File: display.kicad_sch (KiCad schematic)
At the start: 72 parts, among them IC11 SN74LV1T125DBVR, IC6 PCA9517ADP, J1 46756-1001, J2 2129320-3, T1 BSS138APW

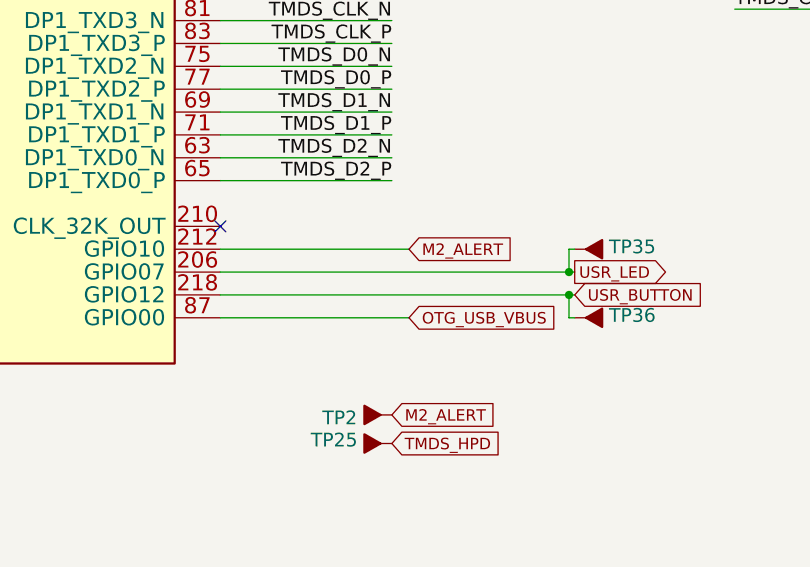
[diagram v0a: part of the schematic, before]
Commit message: Connect OTG VBUS_DET and ID_DET signals to SOM
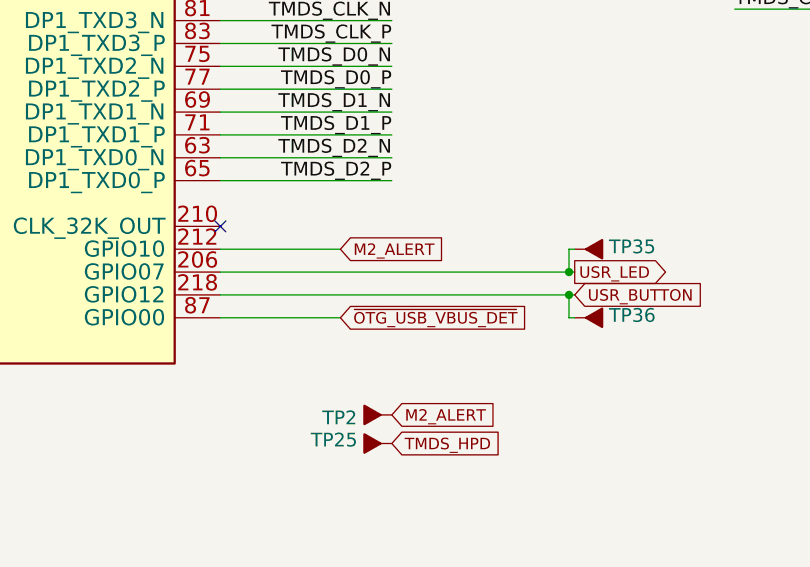
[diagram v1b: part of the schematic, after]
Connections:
- net OTG_USB_VBUS renamed ~{OTG_USB_VBUS_DET}
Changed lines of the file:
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@@
     (stroke (width 0) (type default) (color 0 0 0 0))
   )
-  (wire (pts (xy 63.5 121.92) (xy 84.455 121.92))
+  (wire (pts (xy 63.5 121.92) (xy 76.835 121.92))
     (stroke (width 0) (type default) (color 0 0 0 0))
   )
@@
     (stroke (width 0) (type default) (color 0 0 0 0))
   )
-  (wire (pts (xy 63.5 114.3) (xy 84.455 114.3))
+  (wire (pts (xy 63.5 114.3) (xy 76.835 114.3))
     (stroke (width 0) (type default) (color 0 0 0 0))
   )
@@
     )
   )
-  (global_label "M2_ALERT" (shape input) (at 84.455 114.3 0) (fields_autoplaced)
+  (global_label "M2_ALERT" (shape input) (at 76.835 114.3 0) (fields_autoplaced)
     (effects (font (size 1.27 1.27)) (justify left))
-    (property "Intersheet References" "${INTERSHEET_REFS}" (id 0) (at 0 0 0)
+    (property "Intersheet References" "${INTERSHEET_REFS}" (id 0) (at -7.62 0 0)
       (effects (font (size 1.27 1.27)) hide)
     )
@@
     )
   )
-  (global_label "1V8_SYS" (shape input) (at 236.855 217.805 90) (fields_autoplaced)
+  (global_label "~{OTG_USB_VBUS_DET}" (shape input) (at 76.835 121.92 0) (fields_autoplaced)
     (effects (font (size 1.27 1.27)) (justify left))
-    (property "Intersheet References" "${INTERSHEET_REFS}" (id 0) (at 0 0 0)
-      (effects (font (size 1.27 1.27)) hide)
+    (property "Intersheet References" "${INTERSHEET_REFS}" (id 0) (at 97.7254 121.8406 0)
+      (effects (font (size 1.27 1.27)) (justify left) hide)
     )
   )
-  (global_label "OTG_USB_VBUS" (shape input) (at 84.455 121.92 0) (fields_autoplaced)
+  (global_label "1V8_SYS" (shape input) (at 236.855 217.805 90) (fields_autoplaced)
     (effects (font (size 1.27 1.27)) (justify left))
     (property "Intersheet References" "${INTERSHEET_REFS}" (id 0) (at 0 0 0)

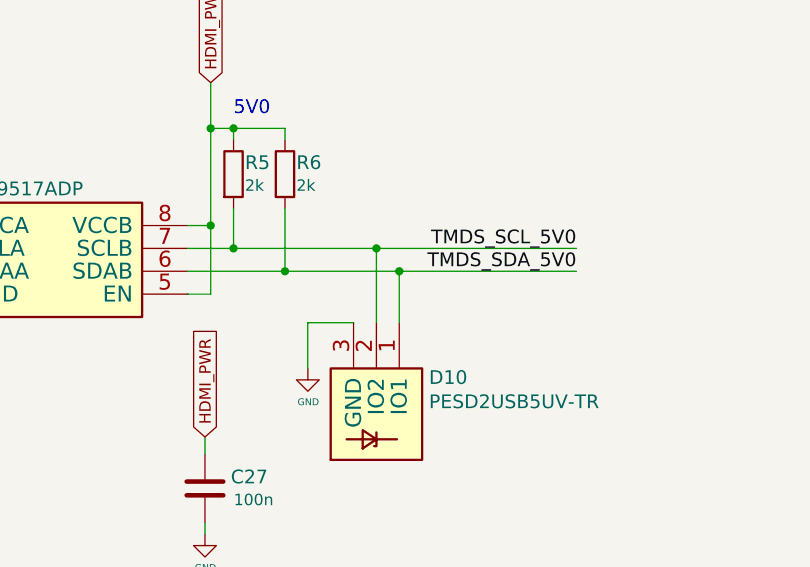
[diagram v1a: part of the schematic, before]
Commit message: Update VBUS_DET label
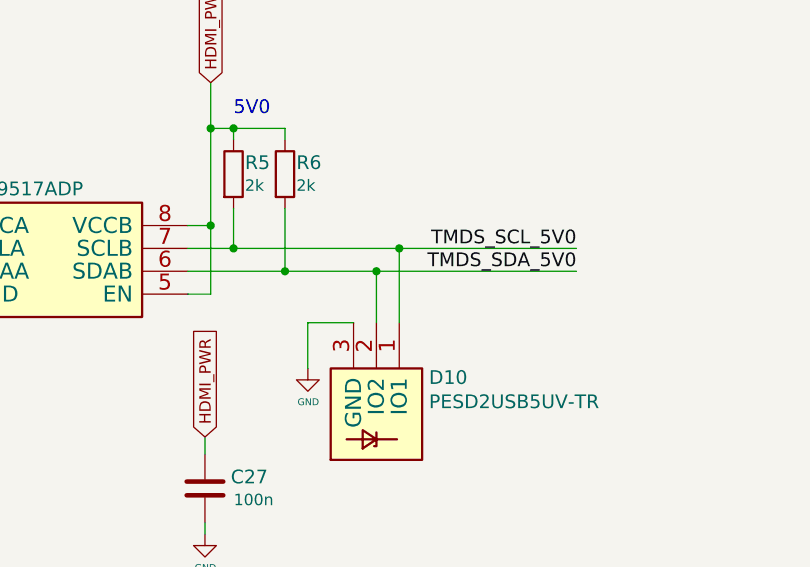
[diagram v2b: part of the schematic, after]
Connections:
- net TMDS_SCL_5V0: now also D10.1 (IO1); no longer D10.2 (IO2)
- net TMDS_SDA_5V0: now also D10.2 (IO2); no longer D10.1 (IO1)
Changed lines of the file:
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@@
   (junction (at 93.345 260.35) (diameter 0) (color 0 0 0 0)
   )
-  (junction (at 367.665 174.625) (diameter 0) (color 0 0 0 0)
-  )
   (junction (at 346.71 169.545) (diameter 0) (color 0 0 0 0)
   )
@@
   (junction (at 300.99 90.805) (diameter 0) (color 0 0 0 0)
   )
+  (junction (at 365.125 174.625) (diameter 0) (color 0 0 0 0)
+  )
+  (junction (at 367.665 172.085) (diameter 0) (color 0 0 0 0)
+  )
   (junction (at 116.205 190.5) (diameter 0) (color 0 0 0 0)
   )
@@
   )
   (junction (at 292.735 90.805) (diameter 0) (color 0 0 0 0)
-  )
-  (junction (at 365.125 172.085) (diameter 0) (color 0 0 0 0)
   )
   (junction (at 354.965 174.625) (diameter 0) (color 0 0 0 0)
@@
     (stroke (width 0) (type default) (color 0 0 0 0))
   )
-  (wire (pts (xy 354.965 174.625) (xy 367.665 174.625))
-    (stroke (width 0) (type default) (color 0 0 0 0))
-  )
   (wire (pts (xy 236.855 218.44) (xy 250.825 218.44))
     (stroke (width 0) (type default) (color 0 0 0 0))
@@
     (stroke (width 0) (type default) (color 0 0 0 0))
   )
+  (wire (pts (xy 365.125 174.625) (xy 365.125 180.34))
+    (stroke (width 0) (type default) (color 0 0 0 0))
+  )
   (wire (pts (xy 313.69 177.165) (xy 313.69 180.34))
     (stroke (width 0) (type default) (color 0 0 0 0))
@@
     (stroke (width 0) (type default) (color 0 0 0 0))
   )
+  (wire (pts (xy 367.665 172.085) (xy 387.35 172.085))
+    (stroke (width 0) (type default) (color 0 0 0 0))
+  )
   (wire (pts (xy 354.33 85.725) (xy 308.61 85.725))
     (stroke (width 0) (type default) (color 0 0 0 0))
   )
-  (wire (pts (xy 365.125 180.34) (xy 365.125 172.085))
-    (stroke (width 0) (type default) (color 0 0 0 0))
-  )
   (wire (pts (xy 90.805 215.9) (xy 149.225 215.9))
     (stroke (width 0) (type default) (color 0 0 0 0))
@@
     (stroke (width 0) (type default) (color 0 0 0 0))
   )
-  (wire (pts (xy 367.665 180.34) (xy 367.665 174.625))
-    (stroke (width 0) (type default) (color 0 0 0 0))
-  )
   (wire (pts (xy 354.33 60.325) (xy 308.61 60.325))
     (stroke (width 0) (type default) (color 0 0 0 0))
@@
     (stroke (width 0) (type default) (color 0 0 0 0))
   )
-  (wire (pts (xy 367.665 174.625) (xy 387.35 174.625))
+  (wire (pts (xy 354.965 174.625) (xy 365.125 174.625))
     (stroke (width 0) (type default) (color 0 0 0 0))
   )
@@
     (stroke (width 0) (type default) (color 0 0 0 0))
   )
-  (wire (pts (xy 349.25 172.085) (xy 365.125 172.085))
-    (stroke (width 0) (type default) (color 0 0 0 0))
-  )
   (wire (pts (xy 118.745 260.35) (xy 116.205 260.35))
     (stroke (width 0) (type default) (color 0 0 0 0))
@@
     (stroke (width 0) (type default) (color 0 0 0 0))
   )
+  (wire (pts (xy 365.125 174.625) (xy 387.35 174.625))
+    (stroke (width 0) (type default) (color 0 0 0 0))
+  )
   (wire (pts (xy 356.235 224.79) (xy 374.65 224.79))
     (stroke (width 0) (type default) (color 0 0 0 0))
@@
     (stroke (width 0) (type default) (color 0 0 0 0))
   )
-  (wire (pts (xy 365.125 172.085) (xy 387.35 172.085))
+  (wire (pts (xy 349.25 172.085) (xy 367.665 172.085))
     (stroke (width 0) (type default) (color 0 0 0 0))
   )
@@
     (stroke (width 0) (type default) (color 0 0 0 0))
   )
+  (wire (pts (xy 367.665 172.085) (xy 367.665 180.34))
+    (stroke (width 0) (type default) (color 0 0 0 0))
+  )

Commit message: Standardize components
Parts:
- removed J2: 2129320-3, jetson-nano-baseboard-footprints:2129320-3, symbol jetson-nano-baseboard:miniDP
- removed R31, R32: R_1M0_0402, jetson-nano-baseboard-footprints:0402-res, symbol jetson-nano-baseboard:R_1M0_0402
- added J2: DisplayPort_Mini_TE_2129320-3, antmicro-footprints:DisplayPort_Mini_TE_2129320-3, symbol antmicroUSBDVIHDMIConnectors:DisplayPort_Mini_TE_2129320-3
- added R31, R32: R_1M_0402, antmicro-footprints:R_0402_1005Metric, symbol antmicroResistors0402:R_1M_0402
- C1, C2, C3, C4: footprint jetson-nano-baseboard-footprints:0402-cap -> antmicro-footprints:C_0402_1005Metric; symbol jetson-nano-baseboard:C_4u7_0402 -> antmicroCapacitors0402:C_4u7_0402; Author (none) -> Antmicro; License (none) -> Apache-2.0; Manufacturer MURATA -> Murata
- C12, C26, C27, C39, C40, C42, C43, C44, C45, C5, C6, C7, C73, C74, C75, C76, C77, C78, C79, C8, C80: footprint jetson-nano-baseboard-footprints:0402-cap -> antmicro-footprints:C_0402_1005Metric; symbol jetson-nano-baseboard:C_100n_0402 -> antmicroCapacitors0402:C_100n_0402; Author (none) -> Antmicro; Dielectric (none) -> X5R; License (none) -> Apache-2.0; MPN 0402X104K6R3CT -> GRM155R61H104KE14D; Manufacturer Walsin -> Murata; Voltage (none) -> 50V
- D10, D11, D12: footprint jetson-nano-baseboard-footprints:SOT-23s -> antmicro-footprints:SOT-23-3; symbol jetson-nano-baseboard:PESD2USB5UV-TR -> antmicroTVSDiodes:PESD2USB5UV-TR; Author (none) -> Antmicro; License (none) -> Apache-2.0; Manufacturer Nexperia -> Nexperia
- D2, D4: footprint jetson-nano-baseboard-footprints:SOD-323 -> antmicro-footprints:D_SOD-323F; symbol jetson-nano-baseboard:diode -> antmicroDiodesRectifiersSingle:1N4148WS; Author (none) -> Antmicro; License (none) -> Apache-2.0
- IC11: footprint jetson-nano-baseboard-footprints:SOT-23-5 -> antmicro-footprints:SOT-23-5; symbol jetson-nano-baseboard:SN74LV1T125DBVR -> antmicroLogicBuffersDriversReceiversTransceivers:SN74LV1T125DBVR; Author (none) -> Antmicro; License (none) -> Apache-2.0
- IC18, IC2: value ~ -> TPD8S009DSMR; footprint jetson-nano-baseboard-footprints:SON-15 -> antmicro-footprints:R-PDSO-N15; symbol jetson-nano-baseboard:TPD8S009 -> antmicroTVSDiodes:TPD8S009DSMR; Author (none) -> Antmicro; License (none) -> Apache-2.0
- IC6: footprint jetson-nano-baseboard-footprints:MSOP-8 -> antmicro-footprints:TSSOP-8_3x3mm_P0.65mm; symbol jetson-nano-baseboard:PCA9517ADP -> antmicroLogicTranslatorsLevelShifters:PCA9517ADP; Author (none) -> Antmicro; License (none) -> Apache-2.0
- J1: value 46756-1001 -> HDMI_Micro-D_46756-1001; footprint jetson-nano-baseboard-footprints:HDMI_Micro-D_Molex_46765-1x01 -> antmicro-footprints:HDMI_Micro-D_Molex_46765-1x01; symbol jetson-nano-baseboard:46756-1001 -> antmicroUSBDVIHDMIConnectors:HDMI_Micro-D_46756-1001; Author (none) -> Antmicro; License (none) -> Apache-2.0
- L10, L8, L9: value BLM18SG121TN1D -> FB_120Z_3A_0603; footprint jetson-nano-baseboard-footprints:0603 -> antmicro-footprints:FB_0603_1608Metric; symbol jetson-nano-baseboard:BLM18SG121TN1D -> antmicroFerriteBeadsandChips:FB_120Z_3A_0603; Author (none) -> Antmicro; License (none) -> Apache-2.0
- M1: value ~ -> Jetson-Nano-new-release; footprint jetson-nano-baseboard-footprints:jetson-nano-connector -> antmicro-footprints:TE_2309413; symbol jetson-nano-baseboard:Jetson-Nano-new-release -> antmicroSoMConnectors:Jetson-Nano-new-release; Author (none) -> Antmicro; License (none) -> Apache-2.0; Manufacturer TE -> TE Connectivity
- R1, R10, R2, R3, R4, R7, R8, R9: footprint jetson-nano-baseboard-footprints:0402-res -> antmicro-footprints:R_0402_1005Metric; symbol jetson-nano-baseboard:R_5R6_0402 -> antmicroResistors0402:R_5R6_0402; Author (none) -> Antmicro; License (none) -> Apache-2.0; MPN ERJ2GEJ5R6X -> CR0402-FX-5R60GLF; Manufacturer PANASONIC_ELECTRONIC_COMPONENTS -> Bourns; Tolerance (none) -> 1%
- R100, R26, R30: footprint jetson-nano-baseboard-footprints:0402-res -> antmicro-footprints:R_0402_1005Metric; symbol jetson-nano-baseboard:R_100k_0402 -> antmicroResistors0402:R_100k_0402; Author (none) -> Antmicro; License (none) -> Apache-2.0; MPN CRCW0402100KFKEDHP -> CR0402-FX-1003GLF; Manufacturer VISHAY -> Bourns; Tolerance (none) -> 1%
- R11, R37, R5, R6, R81, R83, R88: footprint jetson-nano-baseboard-footprints:0402-res -> antmicro-footprints:R_0402_1005Metric; symbol jetson-nano-baseboard:R_2k_0402 -> antmicroResistors0402:R_2k_0402; Author (none) -> Antmicro; License (none) -> Apache-2.0; MPN CRCW04022K00FKED -> CR0402-FX-2001GLF; Manufacturer VISHAY -> Bourns; Tolerance (none) -> 1%
- R12, R82, R98, R99: footprint jetson-nano-baseboard-footprints:0402-res -> antmicro-footprints:R_0402_1005Metric; symbol jetson-nano-baseboard:R_0R_0402 -> antmicroResistors0402:R_0R_0402; Author (none) -> Antmicro; Current (none) -> 1A; License (none) -> Apache-2.0; Manufacturer PANASONIC -> Panasonic
- T1: value BSS138APW -> BSS138PW; footprint jetson-nano-baseboard-footprints:SC70-3 -> antmicro-footprints:SC70-3; symbol jetson-nano-baseboard:BSS138APW -> antmicroTransistorsFETsMOSFETsSingle:BSS138PW; Author (none) -> Antmicro; License (none) -> Apache-2.0; Manufacturer ON Semiconductor -> Nexperia
- TP2, TP25, TP26, TP33, TP34, TP35, TP36: value ~ -> TP_1.5mm_SMD; footprint jetson-nano-baseboard-footprints:TP-R-1.5 -> antmicro-footprints:TP_SMD_1.5mm; symbol jetson-nano-baseboard:Testpad -> antmicroTestPoints:TP_1.5mm_SMD; Author (none) -> Antmicro; License (none) -> Apache-2.0
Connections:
- net DP_CEC: now also J2.6 (CONFIG2), R32.1
- net DP_HPD_IN: now also R100.1, J2.2 (HOTPLUG); no longer R100.2
- net DP_MODE: now also J2.4 (CONFIG1), R31.1
- net EDP_C_AUX_C_N: now also J2.18 (AUX_N)
- net EDP_C_AUX_C_P: now also R30.1, J2.16 (AUX_P); no longer R30.2
- net GND: now also C1.2, C2.2, C27.2, C3.2, C4.2, R100.2, R12.2, R30.2, J2.1 (GND), J2.13 (GND), J2.14 (GND), J2.19 (GND), J2.21 (SH), J2.22 (SH), J2.23 (SH), J2.24 (SH), J2.7 (GND), J2.8 (GND), R31.2, R32.2; no longer C1.1, C2.1, C27.1, C3.1, C4.1, R100.1, R12.1, R30.1
- net HDMI_PWR: now also C27.1; no longer C27.2
- net ML_C_LANE0_N: now also J2.5 (TXD0_N)
- net ML_C_LANE0_P: now also J2.3 (TXD0_P)
- net ML_C_LANE1_N: now also J2.11 (TXD1_N)
- net ML_C_LANE1_P: now also J2.9 (TXD1_P)
- net ML_C_LANE2_N: now also J2.17 (TXD2_N)
- net ML_C_LANE2_P: now also J2.15 (TXD2_P)
- net ML_C_LANE3_N: now also J2.12 (TXD3_N)
- net ML_C_LANE3_P: now also J2.10 (TXD3_P)
- net TMDS_HPD_IN: now also R82.2; no longer R82.1
- net TMDS_SCL: now also R98.1; no longer R98.2
- net TMDS_SDA: now also R99.1; no longer R99.2
- net at IC6.2 (SCLA), R81.2: now also R98.2; no longer R98.1
- net at IC6.3 (SDAA), R11.2: now also R99.2; no longer R99.1
- net at R83.1, T1.1 (G): now also R82.1; no longer R82.2
- net at J1.16 (GND): now also R12.1; no longer R12.2
- new net: C3.1, C4.1, D2.K, J2.20 (DP_PWR)
- new net: C1.1, C2.1, D4.K, J1.19 (+5V)
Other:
- note removed: "1V8"
- moved on the sheet: C1, C12, C2, C26, C27, C3, C39, C4, C40, C42, C43, C44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
